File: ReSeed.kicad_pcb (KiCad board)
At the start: 2 copper layers, 60.8 x 99.9 mm, 50 parts, among them CN1 EDGE_CONNECTOR, CN2 AUDIO_OUT, CN3 AUDIO_IN, CN4 DB9_MALE, Q1 BC549C, SW1 SW_DIGIFIX, U1 MOS_8580, U2 CD74HCT4520E, U3 74HCT245, U4 GAL16V8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

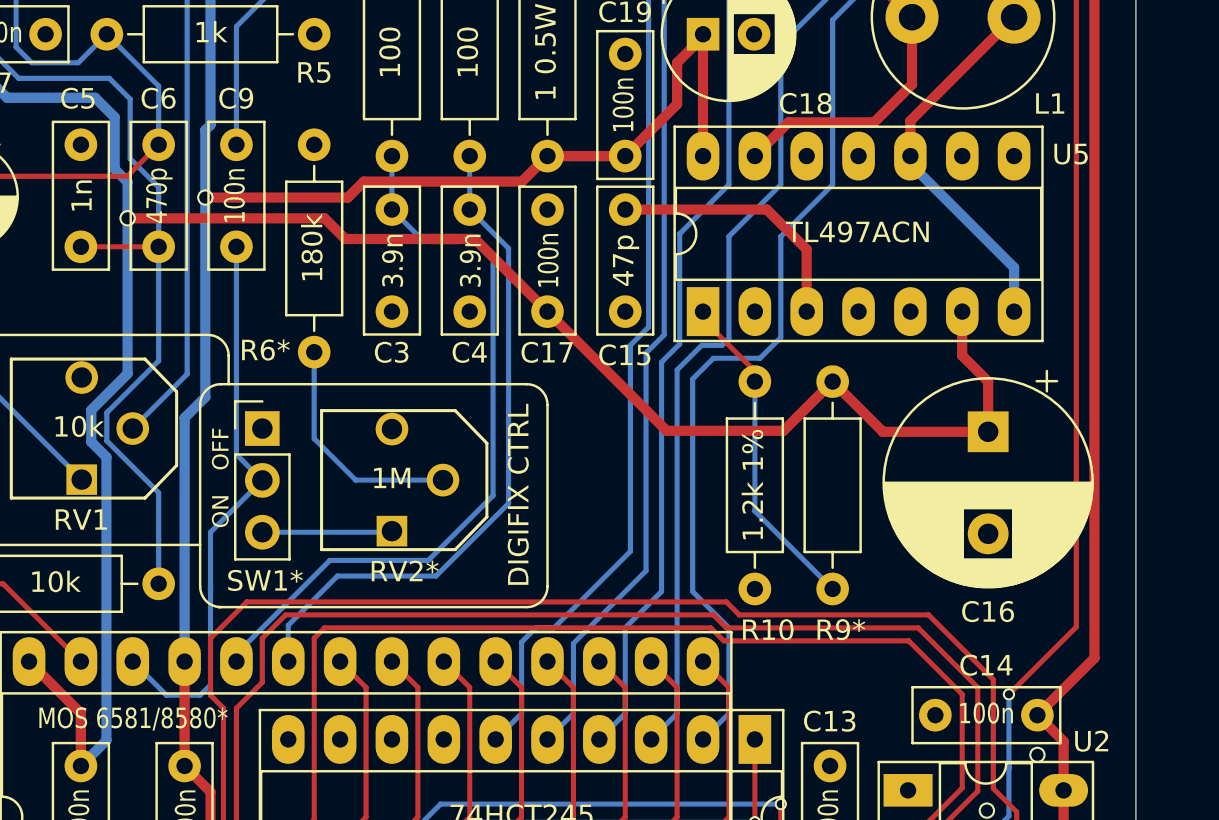
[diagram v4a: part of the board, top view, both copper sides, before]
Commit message: Move some tracks
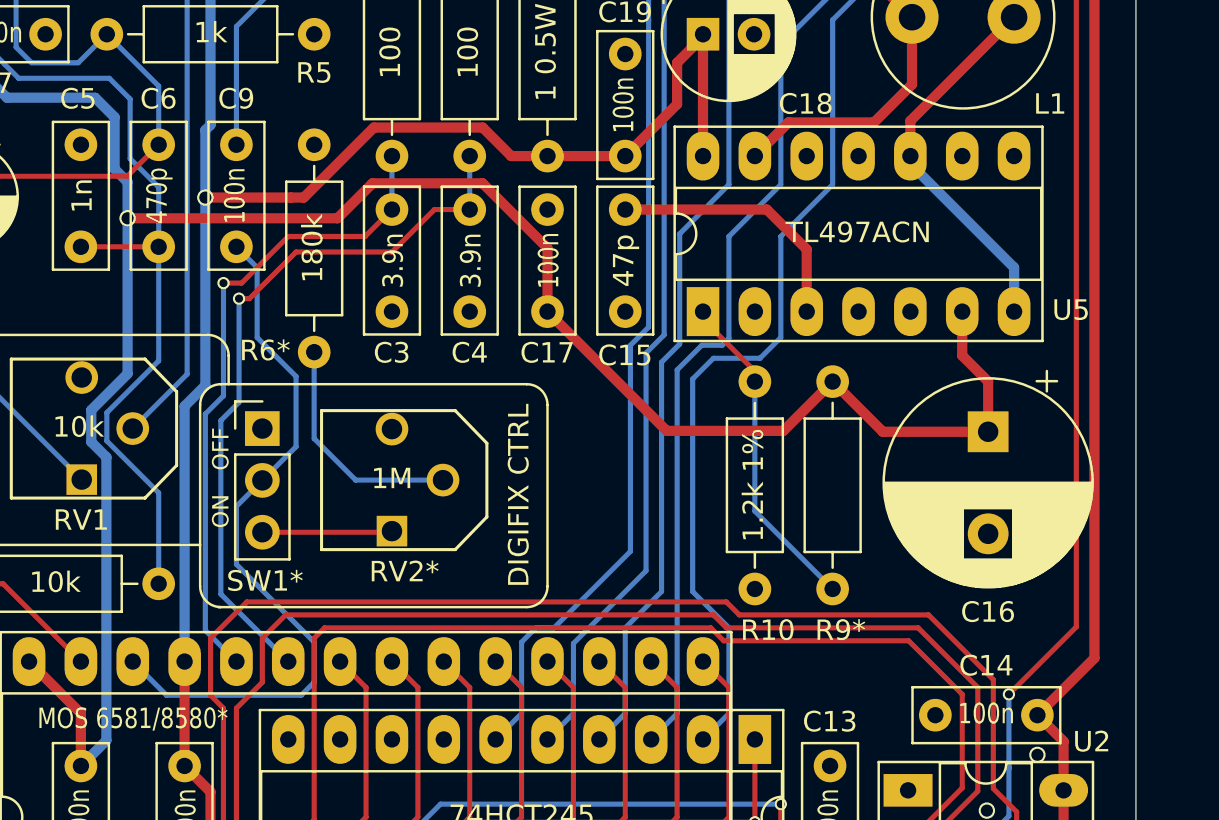
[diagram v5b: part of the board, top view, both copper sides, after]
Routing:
- net /audio_in: track 30.0 -> 35.2 mm
- net Net-(C3-Pad1): track 36.4 -> 31.9 mm, vias 0 -> 1
- net Net-(C4-Pad1): track 32.9 -> 35.2 mm, vias 0 -> 1
- net +9V: track 111.4 -> 113.3 mm
- net +5V: track 268.7 -> 269.9 mm

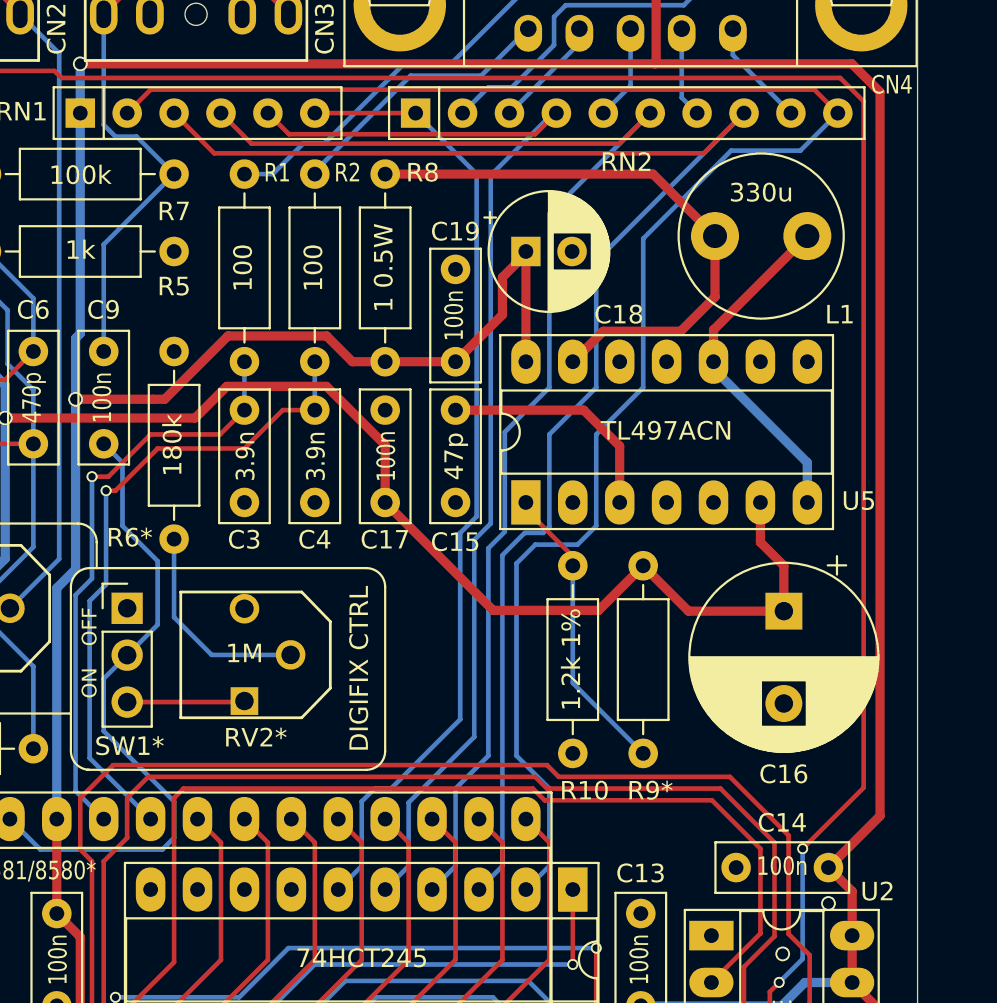
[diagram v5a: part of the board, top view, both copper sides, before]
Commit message: WIP - Add footprint for MT3608-based regulator modules from China
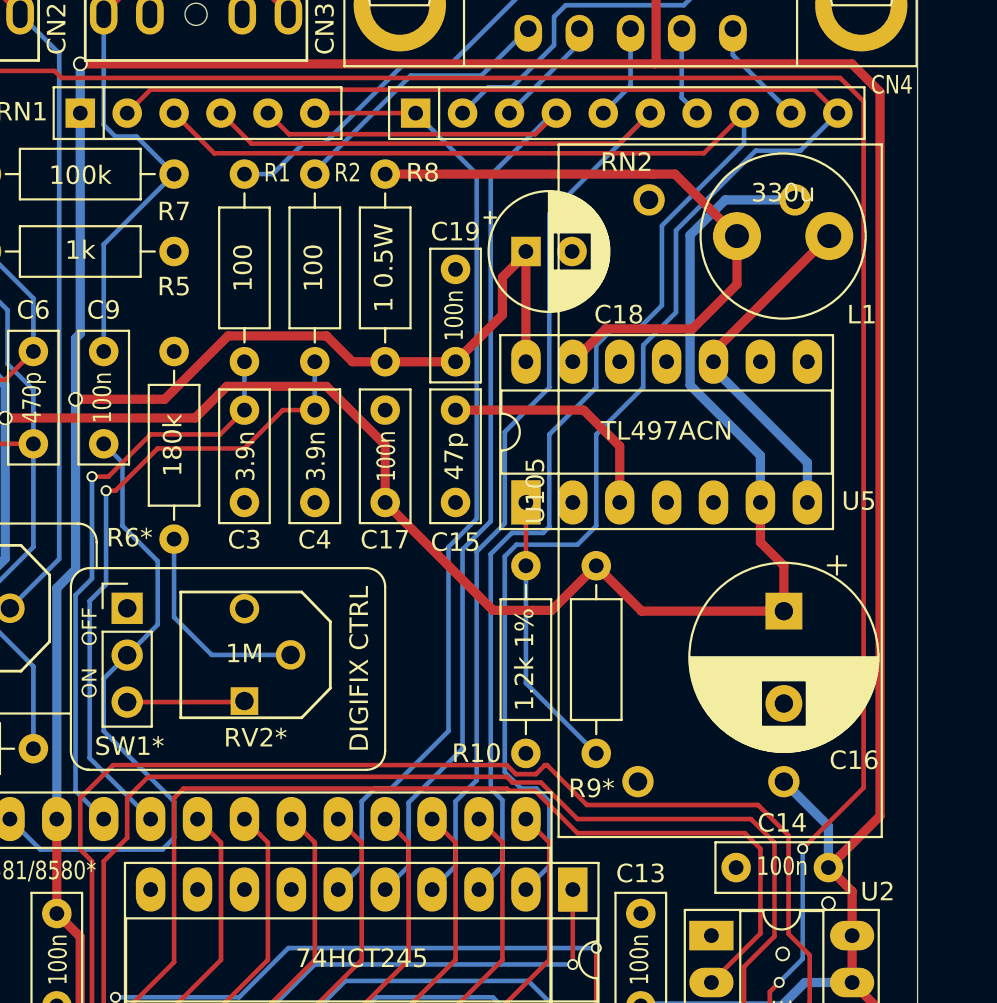
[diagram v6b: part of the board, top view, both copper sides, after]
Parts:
- added U105: STEPUP_MT3608, ReSeed:ChineseUpstepperMT3608Style, F.Cu at (171.9, 83.4)
- moved R10 2.54 mm to (161.4, 97.7)
- moved R9 2.54 mm to (165.2, 97.7)
- moved L1 1.19 mm to (177.8, 69.7)
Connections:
- CN1 pad 10: (no net) -> Net-(CN1-Pad10)
- CN1 pad 11: (no net) -> Net-(CN1-Pad11)
- CN1 pad 13: (no net) -> Net-(CN1-Pad13)
- CN1 pad 22: (no net) -> Net-(CN1-Pad22)
- CN1 pad 4: (no net) -> Net-(CN1-Pad4)
- CN1 pad 6: (no net) -> Net-(CN1-Pad6)
- CN1 pad 7: (no net) -> Net-(CN1-Pad7)
- CN1 pad 8: (no net) -> Net-(CN1-Pad8)
- CN1 pad 9: (no net) -> Net-(CN1-Pad9)
- CN1 pad AA: (no net) -> Net-(CN1-PadAA)
- CN1 pad B: (no net) -> Net-(CN1-PadB)
- CN1 pad BB: (no net) -> Net-(CN1-PadBB)
- CN1 pad D: (no net) -> Net-(CN1-PadD)
- CN1 pad E: (no net) -> Net-(CN1-PadE)
- CN1 pad Z: (no net) -> Net-(CN1-PadZ)
- CN2 pad RN: (no net) -> Net-(CN2-PadRN)
- CN3 pad RN: (no net) -> Net-(CN3-PadRN)
- RV2 pad 3: (no net) -> Net-(RV2-Pad3)
- SW1 pad 1: (no net) -> Net-(SW1-Pad1)
- U2 pad 11: (no net) -> Net-(U2-Pad11)
- U2 pad 12: (no net) -> Net-(U2-Pad12)
- U2 pad 13: (no net) -> Net-(U2-Pad13)
- U2 pad 14: (no net) -> Net-(U2-Pad14)
- U2 pad 4: (no net) -> Net-(U2-Pad4)
- U2 pad 5: (no net) -> Net-(U2-Pad5)
- U2 pad 6: (no net) -> Net-(U2-Pad6)
- U4 pad 11: (no net) -> Net-(U4-Pad11)
- U5 pad 11: (no net) -> Net-(U5-Pad11)
- U5 pad 12: (no net) -> Net-(U5-Pad12)
- U5 pad 9: (no net) -> Net-(U5-Pad9)
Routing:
- net +9V: track 113.3 -> 135.9 mm
- net +5V: track 269.9 -> 275.5 mm
- net Net-(L1-Pad2): track 31.7 -> 33.7 mm
- net Net-(RN1-Pad3): track 81.6 -> 83.3 mm
- net Net-(R10-Pad2): track 16.2 -> 15.2 mm
- net Net-(RN1-Pad2): track 93.6 -> 94.4 mm

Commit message: Routing completed - Need @kinmami's opinion on it
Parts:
- moved R9 10.9 mm to (157.6, 89.9), turned to 0 degrees
- moved R10 7.54 mm to (167.8, 93.6), turned to 180 degrees
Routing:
- net Net-(RN1-Pad2): track 94.4 -> 90.7 mm
- net Net-(R10-Pad2): track 15.2 -> 12.3 mm, vias 0 -> 1
- net +9V: track 135.9 -> 138.1 mm
- net Net-(RN1-Pad3): track 83.3 -> 81.8 mm
- net Net-(C15-Pad1): vias 0 -> 1

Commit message: Move track
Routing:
- net Net-(RN1-Pad6): track 52.6 -> 52.1 mm
